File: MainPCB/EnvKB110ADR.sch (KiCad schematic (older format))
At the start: 240 parts, among them SW1 Boot Mode, SW2 Reset Switch, U1 XC6206PxxxMR, U2 STM32F411CEUx, X1 ECS-2520MV-xxx-xx

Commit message: See List
- Added ANSI support
- redone sections of the board to fit ansi support
- edited all footprints to have through holes so they can be connected on both sides.
- probably a bunch of other shite
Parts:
- added D_ANSI_1: SOD-123, Diode_SMD:D_SOD-123, symbol Device:D_Small
- added K_ANSI_1, K_ANSI_2: KEYSW, MX_Only:MXOnly-2.25U-Hotswap, symbol MX_Alps_Hybrid:MX-NoLED
- added K_ANSI_3: KEYSW, MX_Only:MXOnly-1.5U-Hotswap, symbol MX_Alps_Hybrid:MX-NoLED
- H1, H10, H2, H3, H4, H5, H6, H8, H9: symbol Mechanical:MountingHole -> Mechanical:MountingHole_Pad
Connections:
- wire segments 453 -> 476
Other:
- moved on the sheet: D_62, K_62

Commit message: more progress, working on column traces.
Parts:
- SW1, SW2: footprint Button_Switch_SMD:SW_DIP_SPSTx01_Slide_6.7x4.1mm_W6.73mm_P2.54mm_LowProfile_JPin -> Button_Switch_SMD:SW_Push_SPST_NO_Alps_SKRK
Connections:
- net GND: now also U2.23 (VSS), U2.35 (VSS), U2.47 (VSS)

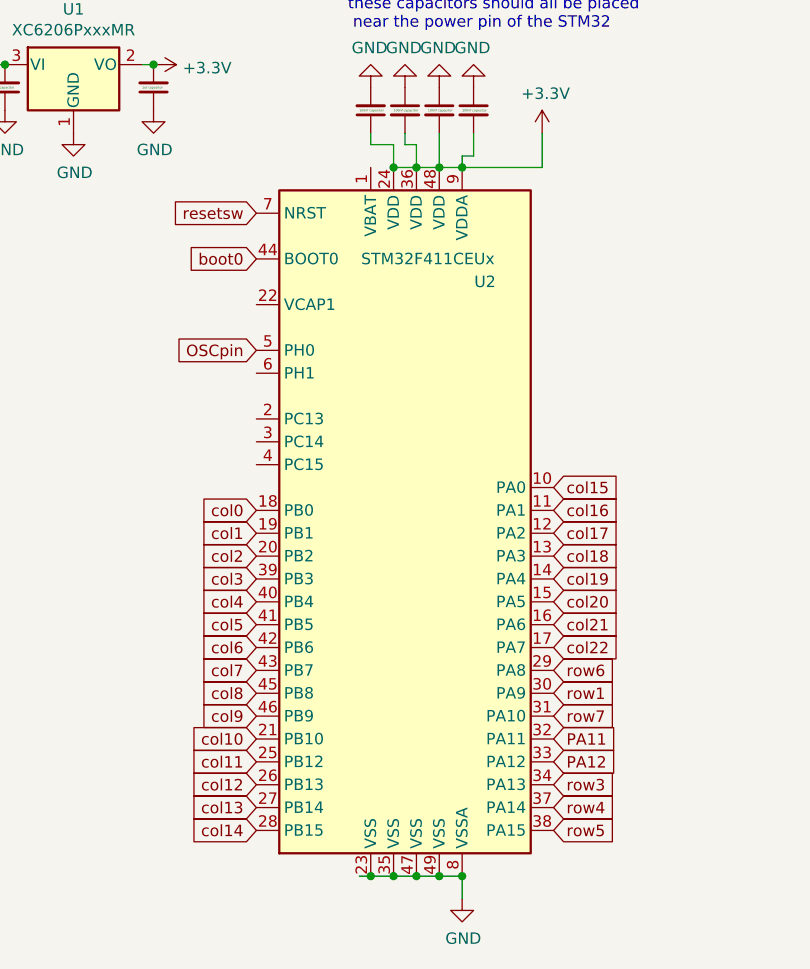
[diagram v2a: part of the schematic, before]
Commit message: finished up traces and added a cat silkscreen.
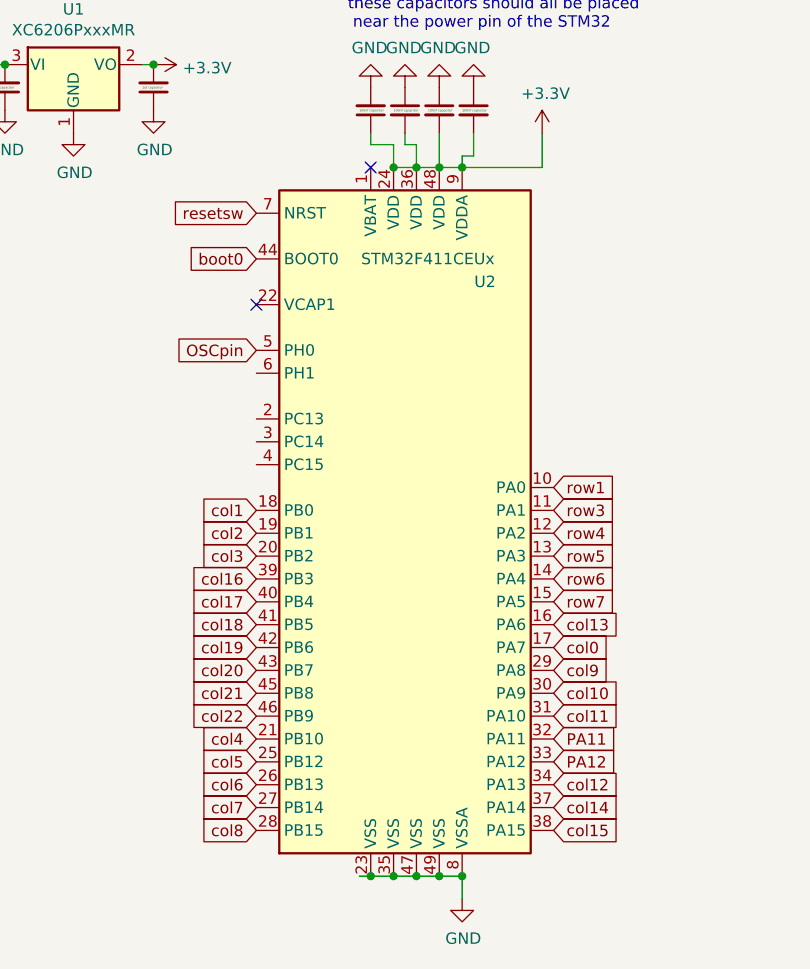
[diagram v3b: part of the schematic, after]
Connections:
- net col0: now also U2.17 (PA7); no longer U2.18 (PB0)
- net col1: now also U2.18 (PB0); no longer U2.19 (PB1)
- net col10: now also U2.30 (PA9); no longer U2.21 (PB10)
- net col11: now also U2.31 (PA10); no longer U2.25 (PB12)
- net col12: now also U2.34 (PA13); no longer U2.26 (PB13)
- net col13: now also U2.16 (PA6); no longer U2.27 (PB14)
- net col14: now also U2.37 (PA14); no longer U2.28 (PB15)
- net col15: now also U2.38 (PA15); no longer U2.10 (PA0)
- net col16: now also U2.39 (PB3); no longer U2.11 (PA1)
- net col17: now also U2.40 (PB4); no longer U2.12 (PA2)
- net col18: now also U2.41 (PB5); no longer U2.13 (PA3)
- net col19: now also U2.42 (PB6); no longer U2.14 (PA4)
- net col2: now also U2.19 (PB1); no longer U2.20 (PB2)
- net col20: now also U2.43 (PB7); no longer U2.15 (PA5)
- net col21: now also U2.45 (PB8); no longer U2.16 (PA6)
- net col22: now also U2.46 (PB9); no longer U2.17 (PA7)
- net col3: now also U2.20 (PB2); no longer U2.39 (PB3)
- net col4: now also U2.21 (PB10); no longer U2.40 (PB4)
- net col5: now also U2.25 (PB12); no longer U2.41 (PB5)
- net col6: now also U2.26 (PB13); no longer U2.42 (PB6)
- net col7: now also U2.27 (PB14); no longer U2.43 (PB7)
- net col8: now also U2.28 (PB15); no longer U2.45 (PB8)
- net col9: now also U2.29 (PA8); no longer U2.46 (PB9)
- net row1: now also U2.10 (PA0); no longer U2.30 (PA9)
- net row3: now also U2.11 (PA1); no longer U2.34 (PA13)
- net row4: now also U2.12 (PA2); no longer U2.37 (PA14)
- net row5: now also U2.13 (PA3); no longer U2.38 (PA15)
- net row6: now also U2.14 (PA4); no longer U2.29 (PA8)
- net row7: now also U2.15 (PA5); no longer U2.31 (PA10)
- no-connect marks 0 -> 2
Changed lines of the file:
@@
 	1    0    0    -1
 $EndComp
+Text GLabel 14000 11950 2    50   Input ~ 0
+col0
 Text GLabel 12700 11350 0    50   Input ~ 0
-col0
+col1
 Text GLabel 12700 11450 0    50   Input ~ 0
-col1
+col2
 Text GLabel 12700 11550 0    50   Input ~ 0
-col2
+col3
+Text GLabel 12700 12350 0    50   Input ~ 0
+col4
+Text GLabel 12700 12450 0    50   Input ~ 0
+col5
+Text GLabel 12700 12550 0    50   Input ~ 0
+col6
+Text GLabel 12700 12650 0    50   Input ~ 0
+col7
+Text GLabel 12700 12750 0    50   Input ~ 0
+col8
+Text GLabel 14000 12050 2    50   Input ~ 0
+col9
+Text GLabel 14000 12150 2    50   Input ~ 0
+col10
+Text GLabel 14000 12250 2    50   Input ~ 0
+col11
+Text GLabel 14000 12550 2    50   Input ~ 0
+col12
+Text GLabel 14000 11850 2    50   Input ~ 0
+col13
+Text GLabel 14000 12650 2    50   Input ~ 0
+col14
+Text GLabel 14000 12750 2    50   Input ~ 0
+col15
 Text GLabel 12700 11650 0    50   Input ~ 0
-col3
+col16
 Text GLabel 12700 11750 0    50   Input ~ 0
-col4
+col17
 Text GLabel 12700 11850 0    50   Input ~ 0
-col5
+col18
 Text GLabel 12700 11950 0    50   Input ~ 0
-col6
+col19
 Text GLabel 12700 12050 0    50   Input ~ 0
-col7
+col20
 Text GLabel 12700 12150 0    50   Input ~ 0
-col8
+col21
 Text GLabel 12700 12250 0    50   Input ~ 0
-col9
-Text GLabel 12700 12350 0    50   Input ~ 0
-col10
-Text GLabel 12700 12450 0    50   Input ~ 0
-col11
-Text GLabel 12700 12550 0    50   Input ~ 0
-col12
-Text GLabel 12700 12650 0    50   Input ~ 0
-col13
-Text GLabel 12700 12750 0    50   Input ~ 0
-col14
+col22
 Text GLabel 14000 11250 2    50   Input ~ 0
-col15
+row1
 Text GLabel 14000 11350 2    50   Input ~ 0
-col16
+row3
 Text GLabel 14000 11450 2    50   Input ~ 0
-col17
+row4
 Text GLabel 14000 11550 2    50   Input ~ 0
-col18
+row5
 Text GLabel 14000 11650 2    50   Input ~ 0
-col19
+row6
 Text GLabel 14000 11750 2    50   Input ~ 0
-col20
-Text GLabel 14000 11850 2    50   Input ~ 0
-col21
-Text GLabel 14000 11950 2    50   Input ~ 0
-col22
-Text GLabel 14000 12150 2    50   Input ~ 0
-row1
-Text GLabel 14000 12550 2    50   Input ~ 0
-row3
-Text GLabel 14000 12650 2    50   Input ~ 0
-row4
-Text GLabel 14000 12750 2    50   Input ~ 0
-row5
-Text GLabel 14000 12050 2    50   Input ~ 0
-row6
-Text GLabel 14000 12250 2    50   Input ~ 0
 row7
 Wire Wire Line
@@
 Wire Wire Line
 	13400 12950 13500 12950
+NoConn ~ 13200 9850
+NoConn ~ 12700 10450
 $EndSCHEMATC

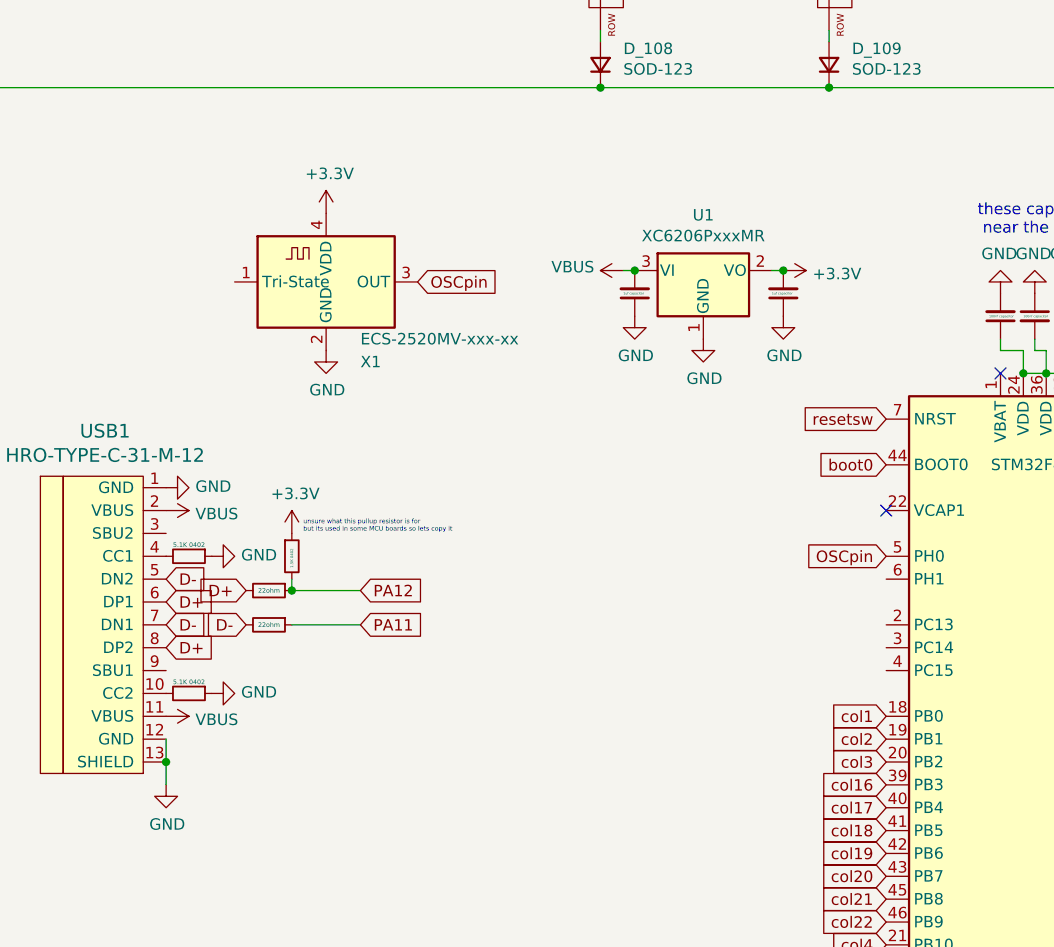
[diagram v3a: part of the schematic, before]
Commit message: changed oscillator for crystal, re-added libraries, made change in PCBNew
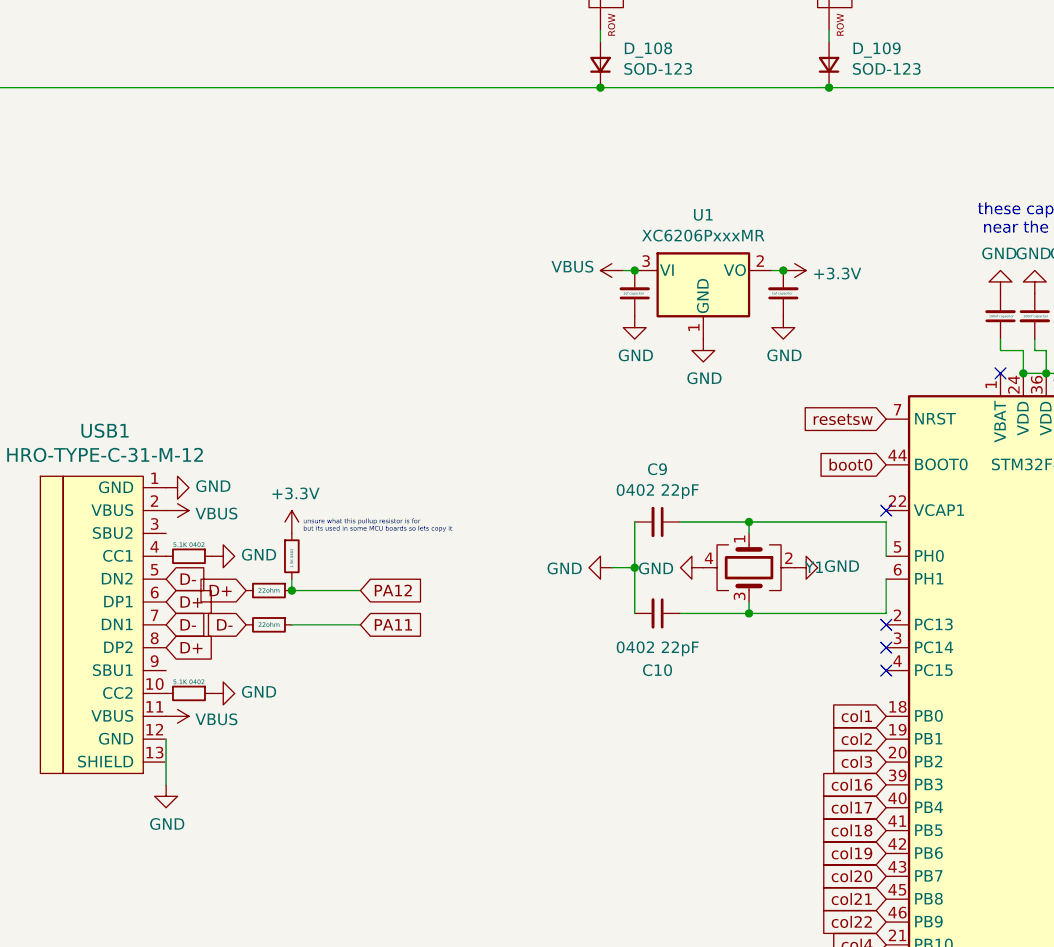
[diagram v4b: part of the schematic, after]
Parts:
- removed X1: ECS-2520MV-xxx-xx, Oscillator:Oscillator_SMD_ECS_2520MV-xxx-xx-4Pin_2.5x2.0mm, symbol Oscillator:ECS-2520MV-xxx-xx
- added C10, C9: 0402 22pF, Capacitor_SMD:C_0402_1005Metric, symbol Device:C_Small
- added Y1: 3225_4P 32.768khz, Crystal:Crystal_SMD_3225-4Pin_3.2x2.5mm, symbol Device:Crystal_GND24
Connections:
- net GND: now also C10.2, C9.2, Y1.2, Y1.4; no longer USB1.13 (SHIELD)
- net at U2.6 (PH1): now also C10.1, Y1.3
- net OSCpin: no longer names the net of U2.5 (PH0)
- net OSCpin: now also C9.1, Y1.1
- no-connect marks 2 -> 5
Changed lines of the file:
@@
 	1    0    0    -1
 $EndComp
-Wire Wire Line
-	9550 11550 9550 11650
-Wire Wire Line
-	9550 11450 9550 11550
-Connection ~ 9550 11550
 $Comp
 L power:GND #PWR0112
@@
 F 3 "" H 11900 9700 50  0001 C CNN
 	1    11900 9700
-	1    0    0    -1
-$EndComp
-$Comp
-L Oscillator:ECS-2520MV-xxx-xx X1
-U 1 1 60E5B405
-P 10250 9450
-F 0 "X1" H 10400 9100 50  0000 L CNN
-F 1 "ECS-2520MV-xxx-xx" H 10400 9200 50  0000 L CNN
-F 2 "Oscillator:Oscillator_SMD_ECS_2520MV-xxx-xx-4Pin_2.5x2.0mm" H 10700 9100 50  0001 C CNN
-F 3 "https://www.ecsxtal.com/store/pdf/ECS-2520MV.pdf" H 10075 9575 50  0001 C CNN
-	1    10250 9450
-	1    0    0    -1
-$EndComp
-Text GLabel 10650 9450 2    50   Input ~ 0
-OSCpin
-Text GLabel 12700 10650 0    50   Input ~ 0
-OSCpin
-$Comp
-L power:+3.3V #PWR01
-U 1 1 60E980B3
-P 10250 9150
-F 0 "#PWR01" H 10250 9000 50  0001 C CNN
-F 1 "+3.3V" H 10265 9323 50  0000 C CNN
-F 2 "" H 10250 9150 50  0001 C CNN
-F 3 "" H 10250 9150 50  0001 C CNN
-	1    10250 9150
-	1    0    0    -1
-$EndComp
-$Comp
-L power:GND #PWR04
-U 1 1 60E99EB6
-P 10250 9750
-F 0 "#PWR04" H 10250 9500 50  0001 C CNN
-F 1 "GND" H 10255 9577 50  0000 C CNN
-F 2 "" H 10250 9750 50  0001 C CNN
-F 3 "" H 10250 9750 50  0001 C CNN
-	1    10250 9750
 	1    0    0    -1
 $EndComp
@@
 NoConn ~ 13200 9850
 NoConn ~ 12700 10450
+$Comp
+L Device:Crystal_GND24 Y1
+U 1 1 6157D500
+P 12100 10700
+F 0 "Y1" V 12100 10944 50  0000 L CNN
+F 1 "3225_4P 32.768khz" V 12145 10944 50  0001 L CNN
+F 2 "Crystal:Crystal_SMD_3225-4Pin_3.2x2.5mm" H 12100 10700 50  0001 C CNN
+F 3 "~" H 12100 10700 50  0001 C CNN
+	1    12100 10700
+	0    1    1    0
+$EndComp
+Wire Wire Line
+	12700 10650 12700 10500
+Wire Wire Line
+	12700 10500 12100 10500
+Wire Wire Line
+	12100 10500 12100 10550
+Wire Wire Line
+	12100 10500 11800 10500
+Connection ~ 12100 10500
+$Comp
+L Device:C_Small C10
+U 1 1 616BE7BD
+P 11700 10900
+F 0 "C10" V 11450 10900 50  0000 C CNN
+F 1 "0402 22pF" V 11550 10900 50  0000 C CNN
+F 2 "Capacitor_SMD:C_0402_1005Metric" H 11700 10900 50  0001 C CNN
+F 3 "~" H 11700 10900 50  0001 C CNN
+	1    11700 10900
+	0    1    -1   0
+$EndComp
+$Comp
+L Device:C_Small C9
+U 1 1 616BF174
+P 11700 10500
+F 0 "C9" V 11929 10500 50  0000 C CNN
+F 1 "0402 22pF" V 11838 10500 50  0000 C CNN
+F 2 "Capacitor_SMD:C_0402_1005Metric" H 11700 10500 50  0001 C CNN
+F 3 "~" H 11700 10500 50  0001 C CNN
+	1    11700 10500
+	0    1    -1   0
+$EndComp
+$Comp
+L power:GND #PWR0118
+U 1 1 616C0646
+P 11900 10700
+F 0 "#PWR0118" H 11900 10450 50  0001 C CNN
+F 1 "GND" V 11905 10572 50  0000 R CNN
+F 2 "" H 11900 10700 50  0001 C CNN
+F 3 "" H 11900 10700 50  0001 C CNN
+	1    11900 10700
+	0    1    1    0
+$EndComp
+$Comp
+L power:GND #PWR0119
+U 1 1 616C18A1
+P 12300 10700
+F 0 "#PWR0119" H 12300 10450 50  0001 C CNN
+F 1 "GND" V 12305 10572 50  0000 R CNN
+F 2 "" H 12300 10700 50  0001 C CNN
+F 3 "" H 12300 10700 50  0001 C CNN
+	1    12300 10700
+	0    -1   -1   0
+$EndComp
+$Comp
+L power:GND #PWR0120
+U 1 1 616C1C2C
+P 11500 10700
+F 0 "#PWR0120" H 11500 10450 50  0001 C CNN
+F 1 "GND" V 11505 10572 50  0000 R CNN
+F 2 "" H 11500 10700 50  0001 C CNN
+F 3 "" H 11500 10700 50  0001 C CNN
+	1    11500 10700
+	0    1    1    0
+$EndComp
+Wire Wire Line
+	12700 10900 12100 10900
+Wire Wire Line
+	12100 10900 12100 10850
+Wire Wire Line
+	12100 10900 11800 10900
+Connection ~ 12100 10900
+Wire Wire Line
+	12700 10750 12700 10900
+Wire Wire Line
+	11600 10900 11600 10700
+Wire Wire Line
+	11600 10700 11500 10700
+Wire Wire Line
+	11600 10700 11600 10500
+Connection ~ 11600 10700
+Wire Wire Line
+	9550 11450 9550 11650
+NoConn ~ 12700 10950
+NoConn ~ 12700 11050
+NoConn ~ 12700 11150
 $EndSCHEMATC

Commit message: Small fixes and corrections
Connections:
- net GND: now also USB1.13 (SHIELD)
- no-connect marks 5 -> 7
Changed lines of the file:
@@
 	1900 900  1900 2150
-Wire Wire Line
-	13150 12950 13200 12950
 Wire Wire Line
 	3900 2150 3900 4150
@@
 	1900 2150 1900 4150
 Connection ~ 13500 12950
-Connection ~ 13200 12950
 Wire Wire Line
 	13200 12950 13300 12950
@@
 	11600 10700 11600 10500
 Connection ~ 11600 10700
-Wire Wire Line
-	9550 11450 9550 11650
 NoConn ~ 12700 10950
 NoConn ~ 12700 11050
 NoConn ~ 12700 11150
+NoConn ~ 9550 11150
+NoConn ~ 9550 10550
+Wire Wire Line
+	9550 11450 9550 11550
+Connection ~ 9550 11550
+Wire Wire Line
+	9550 11550 9550 11650
 $EndSCHEMATC

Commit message: some general changes, might change MCU to RP2040
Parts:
- SW1, SW2: footprint Button_Switch_SMD:SW_Push_SPST_NO_Alps_SKRK -> Button_Switch_SMD:Panasonic_EVQPUJ_EVQPUA
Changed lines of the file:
@@
 F 0 "SW1" H 7600 10135 50  0000 C CNN
 F 1 "Boot Mode" H 7600 10044 50  0000 C CNN
-F 2 "Button_Switch_SMD:SW_Push_SPST_NO_Alps_SKRK" H 7600 10043 50  0001 C CNN
+F 2 "Button_Switch_SMD:Panasonic_EVQPUJ_EVQPUA" H 7600 10043 50  0001 C CNN
 F 3 "~" H 7600 10050 50  0001 C CNN
 	1    7600 9850
@@
 F 0 "SW2" H 7700 10750 50  0000 C CNN
 F 1 "Reset Switch" H 7700 10800 20  0000 C CNN
-F 2 "Button_Switch_SMD:SW_Push_SPST_NO_Alps_SKRK" H 7700 11043 50  0001 C CNN
+F 2 "Button_Switch_SMD:Panasonic_EVQPUJ_EVQPUA" H 7700 11043 50  0001 C CNN
 F 3 "~" H 7700 11050 50  0001 C CNN
 	1    7700 10850
